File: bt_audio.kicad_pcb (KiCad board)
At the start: 2 copper layers, 30 x 41 mm, 77 parts, among them J1 AudioJack4_Ground, J2 Conn_01x02, J3 USB_C_Receptacle_USB2.0, SW1 EVP-BV2C1L000, SW2 EVP-BV2C1L000, SW3 EVP-BV2C1L000, SW4 EVP-BV2C1L000, SW5 EVP-BV2C1L000, SW6 EVP-BV2C1L000, U1 MC_BM83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

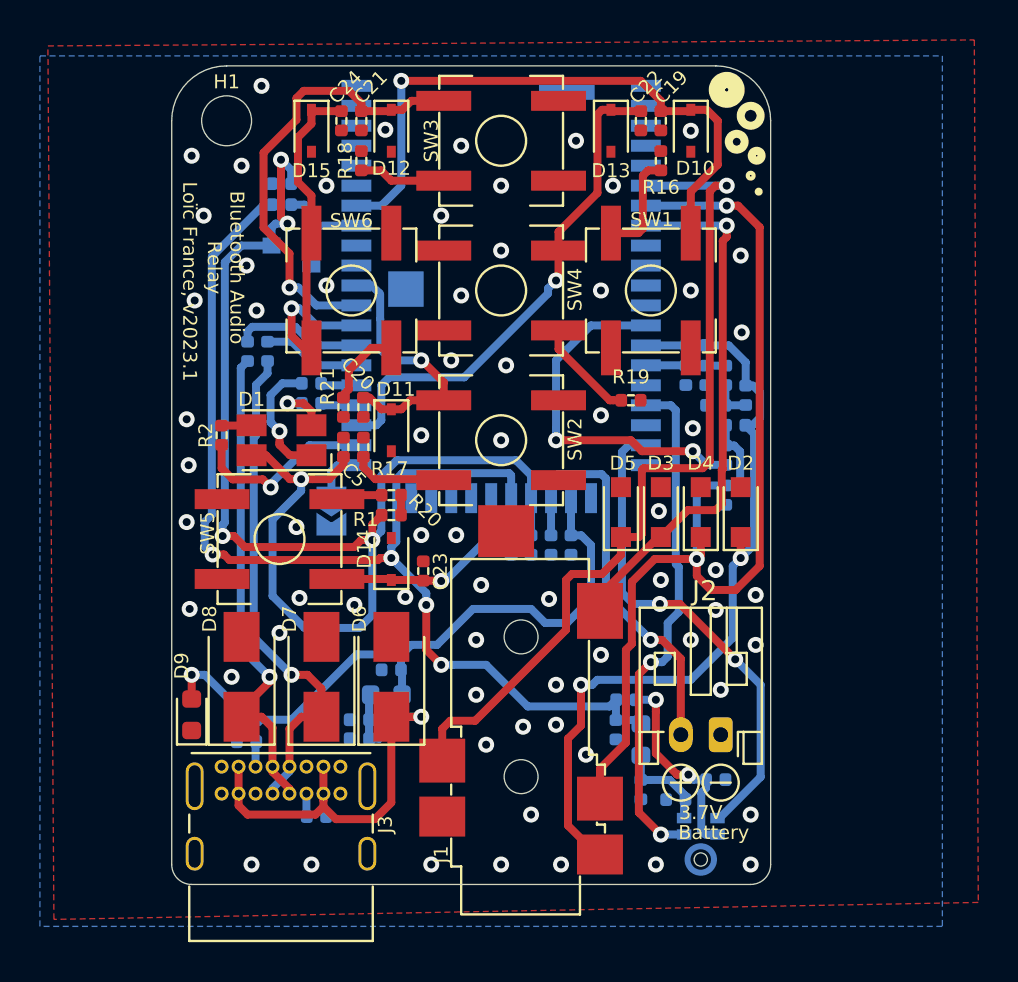
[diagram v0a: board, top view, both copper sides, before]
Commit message: add git url on pcb, add gitignore
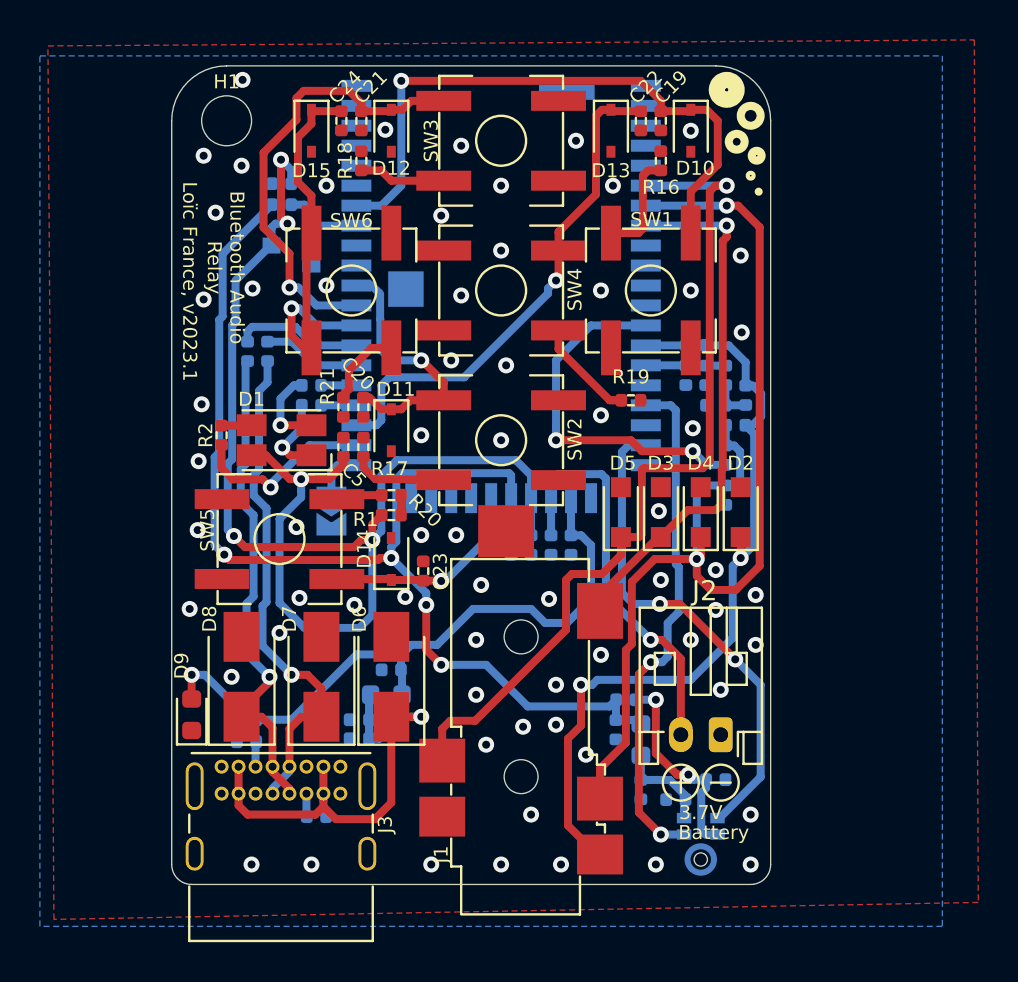
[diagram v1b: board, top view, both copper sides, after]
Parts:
- moved LOGO1 22.2 mm to (88.8, 108.3)
- moved R4 1.10 mm to (82.0, 87.5)
- moved R3 0.90 mm to (82.0, 86.5)
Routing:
- net Net-(D1-Pad1): track 6.30 -> 4.14 mm
- net /SYS_PWR: track 68.8 -> 67.1 mm
- net Net-(D1-Pad4): track 2.78 -> 4.22 mm
- net GND: vias 67 -> 66
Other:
- board text added: "github.com/loicfrance/bluetooth-audio-relay"
